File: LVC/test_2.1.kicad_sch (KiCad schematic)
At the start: 3 parts, among them U1 TL431DBZ

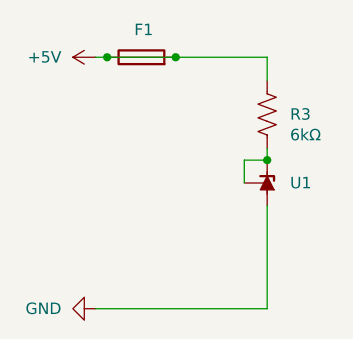
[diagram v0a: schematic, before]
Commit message: Refining Schematics
Refined the visuals of all the schematics to remove values from components. Also removed a redundant schematic.
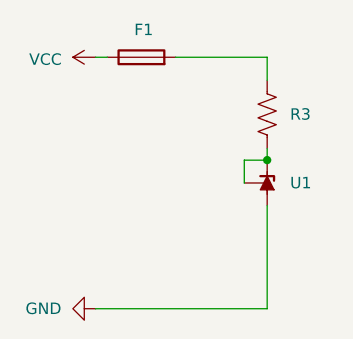
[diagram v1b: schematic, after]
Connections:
- net +5V: no longer F1.2, R3.1
- new net: F1.2, R3.1
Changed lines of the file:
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@@
 	(paper "A4")
-	(junction
-		(at 87.63 44.45)
-		(diameter 0)
-		(color 0 0 0 0)
-	)
 	(junction
 		(at 97.79 55.88)
@@
 		(color 0 0 0 0)
 	)
-	(junction
-		(at 80.01 44.45)
-		(diameter 0)
-		(color 0 0 0 0)
-	)
 	(wire
 		(pts
@@
 		(pts
 			(xy 97.79 46.99) (xy 97.79 44.45)
-		)
-		(stroke
-			(width 0)
-			(type default)
-		)
-	)
-	(wire
-		(pts
-			(xy 80.01 44.45) (xy 87.63 44.45)
 		)
 		(stroke
@@
 		(in_pos_files yes)
 		(dnp no)
-		(fields_autoplaced yes)
-		(property "Reference" "#PWR01"
-			(at 82.55 44.45 0)
-			(hide yes)
+		(property "Reference" "VCC"
+			(at 73.152 44.704 90)
 			(show_name no)
 			(do_not_autoplace no)
@@
 		(property "Value" "+5V"
 			(at 74.93 44.4499 90)
+			(hide yes)
 			(show_name no)
 			(do_not_autoplace no)
@@
 			(project "LVC"
 				(path "/9fe3796c-aa4a-405e-be5a-a1060b4d996f"
-					(reference "#PWR01")
+					(reference "VCC")
 					(unit 1)
 				)
@@
 		(property "Value" "6kΩ"
 			(at 100.33 53.086 0)
-			(show_name no)
-			(do_not_autoplace no)
+			(hide yes)
+			(show_name no)
+			(do_not_autoplace no)
